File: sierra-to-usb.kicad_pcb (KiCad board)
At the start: 4 copper layers, 140 x 100 mm, 367 parts, among them CN1 EM92xx / RM520N M.2 Key-B (67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, J1 TYPE-C-31-M-04, J10 BWSMA-KE-Z001, J11 CONMHF4-SMD-G-T, J12 BWSMA-KE-Z001, J13 CONMHF4-SMD-G-T, J14 BWSMA-KE-Z001, J15 CONMHF4-SMD-G-T, J16 BWSMA-KE-Z001, J17 CONMHF4-SMD-G-T, J18 BWSMA-KE-Z001, J2 TYPE-C-31-M-12, J3 TYPE-C-31-M-12, J4 SWD, J5 Qwiic, J6 Fan, J7 Spare, J8 2250504-1, J9 CONMHF4-SMD-G-T, Q1 2N7002, Q2 2N7002, Q20 FDMS86250, Q21 FDMC2523P, Q22 BSC057N08NS3 G, Q23 BSC057N08NS3 G, Q24 FCX493TA, Q25 FCX493TA, Q3 2N7002, Q30 IRLR7843TRPBF, Q31 IRLR7843TRPBF, Q32 DMG3415U-7, Q33 DMG3415U-7, Q34 2N7002, Q35 2N7002, Q36 BSS138, Q37 BSS138, Q38 BSS138, Q39 2N7002, Q4 2N7002, Q40 BSS138, Q5 2N7002, SW1 DIP-4, SW2 LED_KILL, SW3 BOOTSEL, SW4 RUN, T1 750313355, U1 HD3SS3220RNHR, U10 TPS23730RMTR, U11 93C46, U12 TLV62569DBVR, U13 INA226AIDGSR, U14 INA226AIDGSR, U15 TPS62933FDRLR, U17 AP2112K-3.3TRG1, U19 LM5050MKX-1/NOPB, U2 CH224K, U20 TCMT1107, U21 LM5050MKX-1/NOPB, U22 TL431IDBVR, U23 FOD817DS, U24 RP2040, U25 W25Q128JVS, U26 TMP112AIDRLR, U27 TMP112AIDRLR, U28 SK6805-EC15, U29 TS3A27518EPWR, U3 TPS565201DDCR, U30 ST4SIM-200M, U4 AP2112K-3.3TRG1, U5 AP2112K-1.8TRG1, U8 TS3USB221DRCR, U9 RTL8125BG-CG, Y1 12MHz, Y2 25MHz

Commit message: pcb/rules: match JLCPCB capabilities + calculator-verified impedance geometry
Netclass recovery: commit 777bcae (KiCad session-quit prefs save) had
clobbered the Task-15 netclasses -- DIFF_USB_90/PCIE_85/MDI_100, RF_50,
POE_PRI, POWER were gone, so every .kicad_dru impedance rule AND the
2.5mm PoE moat matched nothing. Restored all 7 classes + 37 patterns
from 59abbed and dropped the orphaned Sig/USB placeholders (their 50SE/
90D tuning profiles kept, re-attached to Default/DIFF_USB_90).

Impedance geometry re-derived on JLCPCB's live calculator (stackup tab
JLC04161H-7628 Standard, 4L/1.6mm, outer 1oz/inner 0.5oz, 2026-07-16),
closing the PRIORITY RF_50 order gate:
  90D  0.24  -> 0.2474 / 0.15   85D 0.27 -> 0.2835 / 0.15
  100D 0.19  -> 0.1826 / 0.15   RF_50 CPWG 0.14 -> 0.3345 / 0.30 gap
  (closed-form CPWG was 2.4x too narrow; would have run ~70+ ohm)
NEW: Default class = 50 ohm SE microstrip 0.3586mm (user request), with
a DRU opt-width rule allowing neck-downs to the 0.09 fab floor.

Board constraint floors set to the live JLCPCB multilayer capability
table (trace/space 0.09, via 0.25/0.15, hole-to-hole 0.2, edge 0.3,
silk 0.15/1.0mm, mask bridge 0.1 via solder_mask_min_width). DRU
Section 3 adds PTH-specific limits (annular 0.15, hole-to-track 0.28,
pad hole-to-hole 0.45) + scoped exemptions for the USB-C C129018
B-row (JLC's own pattern) and same-footprint pad pairs (0.15 floor).

DFM fixes: J1/CN1 locating pegs converted PTH->NPTH (plating would
have shrunk the holes below the pegs); J8 magjack pads shrunk
(13-16: 1.5->1.35, 1: 1.7->1.55, shields 2.4->2.3) to clear 0.04mm
different-net etch gaps. Lib + board both updated.

Gates: nets/footprints/3d pass, ERC 0 errors, DRC 0 in-board errors
(silk warnings + off-board parking-lot items remain, mid-layout).
docs: ordering.md impedance table rewritten, sourcing.md SIM-CD gate
struck (14c), footprint-verification.md deviation notes.

Co-Authored-By: Claude Fable 5 <noreply@anthropic.com>
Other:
- board text added: "IMPEDANCE GEOMETRIES (L1 top, referenced to In1 GND through 0.2104mm/Er4.4 prepreg). SOURCE: JLCPCB live impedance calculator, stackup JLC04161H-7628 (Standard, finished 1.59mm+/-10%), 4L/1.6mm, outer 1oz / inner 0.5oz, verified 2026-07-16 (replaces Task-15 closed-form values; RF_50 closed form was wrong 2.4x -- see .kicad_dru header): DIFF_USB_90 (USB2 SS/D+-): W=0.2474mm gap=0.15mm -> Zdiff 90 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"
- board text removed: "IMPEDANCE GEOMETRIES (L1 top, referenced to In1 GND, H=0.2104mm Er=4.4; computed via IPC-2141 edge-coupled microstrip / grounded-CPW closed form, T=0.05mm finished outer Cu; verify against JLCPCB's live impedance calculator before ordering): DIFF_USB_90 (USB2 SS/D+-): W=0.24mm gap=0.15mm -> Zdiff ~90.2 ohm DIFF_PCIE_85 (M.2 PCIe/REFCLK): W=0.27mm gap=0.15mm -> Zdiff ~85.0 ohm DIFF_MDI_100 (Ethern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"
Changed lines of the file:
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@@
 		)
 		(pad_to_mask_clearance 0)
+		(solder_mask_min_width 0.1)
 		(allow_soldermask_bridges_in_footprints no)
 		(tenting
@@
 			)
 		)
-		(pad "" thru_hole circle
+		(pad "" np_thru_hole circle
 			(at -3.67 -2.54 180)
 			(size 0.8 0.8)
@@
 			(remove_unused_layers no)
 		)
-		(pad "" thru_hole circle
+		(pad "" np_thru_hole circle
 			(at 3.68 -2.54 180)
 			(size 0.8 0.8)
@@
 			)
 		)
-		(pad "" thru_hole circle
+		(pad "" np_thru_hole circle
 			(at -10 1.5)
 			(size 1.1 1.1)
@@
 			(remove_unused_layers no)
 		)
-		(pad "" thru_hole circle
+		(pad "" np_thru_hole circle
 			(at 10 1.5)
 			(size 1.6 1.6)
@@
 		(pad "1" thru_hole roundrect
 			(at 5.08 -7.945 180)
-			(size 1.7 1.7)
+			(size 1.55 1.55)
 			(drill 0.9)
 			(layers "*.Cu" "*.Mask")
@@
 		(pad "13" thru_hole circle
 			(at 5.588 -0.84 180)
-			(size 1.5 1.5)
+			(size 1.35 1.35)
 			(drill 0.9)
 			(layers "*.Cu" "*.Mask")
@@
 		(pad "14" thru_hole circle
 			(at -5.588 -0.84 180)
-			(size 1.5 1.5)
+			(size 1.35 1.35)
 			(drill 0.9)
 			(layers "*.Cu" "*.Mask")
@@
 		(pad "15" thru_hole circle
 			(at 5.588 0.703 180)
-			(size 1.5 1.5)
+			(size 1.35 1.35)
 			(drill 0.9)
 			(layers "*.Cu" "*.Mask")
@@
 		(pad "16" thru_hole circle
 			(at -5.588 0.703 180)
-			(size 1.5 1.5)
+			(size 1.35 1.35)
 			(drill 0.9)
 			(layers "*.Cu" "*.Mask")
@@
 		(pad "SH" thru_hole oval
 			(at -7.166 -6.189 180)
-			(size 2.4 4.6)
+			(size 2.3 4.6)
 			(drill oval 2 4.2)
 			(layers "*.Cu" "*.Mask")
@@
 		(pad "SH" thru_hole oval
 			(at 7.166 -6.189 180)
-			(size 2.4 4.6)
+			(size 2.3 4.6)
 			(drill oval 2 4.2)
 			(layers "*.Cu" "*.Mask")
@@
 		)
 	)
-	(gr_text "IMPEDANCE GEOMETRIES (L1 top, referenced to In1 GND, H=0.2104mm Er=4.4; computed via\nIPC-2141 edge-coupled microstrip / grounded-CPW closed form, T=0.05mm finished outer Cu;\nverify against JLCPCB's live impedance calculator before ordering):\n  DIFF_USB_90  (USB2 SS/D+-):  W=0.24mm  gap=0.15mm  -> Zdiff ~90.2 ohm\n  DIFF_PCIE_85 (M.2 PCIe/REFCLK): W=0.27mm gap=0.15mm -> Zdiff ~85.0 ohm\n  DIFF_MDI_100 (Ethernet MDI): W=0.19mm  gap=0.15mm  -> Zdiff ~100.1 ohm\n  RF_50 (CPWG, ANT/GNSS):      W=0.14mm  ground-gap=0.30mm -> Z0 ~50.0 ohm\nCopper-to-other-net clearance floor for all 4 classes: 0.30mm (see .kicad_dru).\nAlso entered in docs/ordering.md for the JLC order form."
+	(gr_text "IMPEDANCE GEOMETRIES (L1 top, referenced to In1 GND through 0.2104mm/Er4.4 prepreg).\nSOURCE: JLCPCB live impedance calculator, stackup JLC04161H-7628 (Standard, finished 1.59mm+/-10%),\n4L/1.6mm, outer 1oz / inner 0.5oz, verified 2026-07-16 (replaces Task-15 closed-form values;\nRF_50 closed form was wrong 2.4x -- see .kicad_dru header):\n  DIFF_USB_90  (USB2 SS/D+-):  W=0.2474mm  gap=0.15mm  -> Zdiff 90 ohm\n  DIFF_PCIE_85 (M.2 PCIe/REFCLK): W=0.2835mm gap=0.15mm -> Zdiff 85 ohm\n  DIFF_MDI_100 (Ethernet MDI): W=0.1826mm  gap=0.15mm  -> Zdiff 100 ohm\n  RF_50 (CPWG, ANT/GNSS):      W=0.3345mm  ground-gap=0.30mm -> Z0 50 ohm\n  Default (normal signals):    W=0.3586mm microstrip -> Z0 50 ohm (user-requested)\nCopper-to-other-net clearance floor for the 4 controlled classes: 0.30mm (see .kicad_dru).\nAlso entered in docs/ordering.md for the JLC order form (select JLC04161H-7628 + impedance control)."
 		(at -22.87868 70.12132 0)
 		(layer "Cmts.User")

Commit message: pcb: user F8 netlist update (J2/J3->M-04, SIM->XKNANO) + 85D/100D/50CPWG tuning profiles + XKNANO NPTH pegs
- Board: user GUI session applied Update PCB from Schematic (3x TYPE-C-31-M-04,
  2x NanoSIM_XKB_XKNANO-113; stale M-12/CSIM footprints gone). Session quit-save
  also alphabetized netclasses in the .kicad_pro -- values verified intact.
- Tuning profiles completed: 85D (0.2835/0.15), 100D (0.1826/0.15), 50CPWG
  (0.3345) cloned from the session's 50SE/90D templates with JLCPCB-calculator
  geometry; attached to DIFF_PCIE_85 / DIFF_MDI_100 / RF_50. All 7 classes now
  carry matching profiles (POE_PRI/POWER intentionally none).
- XKNANO-113 0.9mm locating pegs converted thru_hole->np_thru_hole (lib+board),
  same easyeda2kicad plated-peg artifact as J1/CN1.
- KNOWN OPEN (user re-placement): SIM1/SIM2 courtyards overlap at old spacing --
  XKNANO body is larger; SIM2 shell pad currently shorts SIM1 UIM1_CLK pad.

Gates: nets/footprints pass; J8/J1/CN1 geometry fixes verified surviving F8.

Co-Authored-By: Claude Fable 5 <noreply@anthropic.com>
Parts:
- J2, J3: value TYPE-C-31-M-12 -> TYPE-C-31-M-04; footprint Connector_USB:USB_C_Receptacle_HRO_TYPE-C-31-M-12 -> sierra-to-usb:USB_C_Receptacle_HRO_TYPE-C-31-M-04
- SIM1, SIM2: value CSIM-H137-7P -> XKNANO-113; footprint sierra-to-usb:NanoSIM_JXTCONN_CSIM-H137-7P -> sierra-to-usb:NanoSIM_XKB_XKNANO-113
- moved T1 80.1 mm to (192.0, 16.5)
- moved J1 74.6 mm to (-33.4, -8.89)
- moved C58 71.7 mm to (-41.6, 0.08)
- moved C59 71.7 mm to (-41.6, 2.59)
- moved C62 71.7 mm to (-41.6, 10.1)
- moved R71 71.7 mm to (-41.6, 17.6)
- moved C60 71.7 mm to (-41.6, 5.10)
- moved C61 71.7 mm to (-41.6, 7.61)
- moved D20 71.7 mm to (-38.1, 1.07)
- moved D21 71.7 mm to (-35.2, 1.07)
- moved D22 71.7 mm to (-32.3, 1.07)
- moved D23 71.7 mm to (-29.4, 1.07)
- moved D24 71.7 mm to (-35.4, 16.4)
- moved R69 71.7 mm to (-41.6, 12.6)
- moved R70 71.7 mm to (-41.6, 15.1)
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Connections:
- SIM1 pad 4: GND -> UIM1_DET
- SIM1 pad 5: UIM1_IO -> GND
- SIM1 pad 6: GND -> unconnected-(SIM1-VPP-Pad6)
- SIM1 pad 7: UIM1_DET -> UIM1_IO
- SIM2 pad 4: GND -> /SIM/UIM2S_DET
- SIM2 pad 5: /SIM/UIM2S_IO -> GND
- SIM2 pad 6: GND -> unconnected-(SIM2-VPP-Pad6)
- SIM2 pad 7: /SIM/UIM2S_DET -> /SIM/UIM2S_IO

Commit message: pcb: layout progress snapshot (user session, pre-resize)
Co-Authored-By: Claude Fable 5 <noreply@anthropic.com>
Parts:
- C116, C117, C118, C119, C120, C121, C122, C123, C124, C125, U10: moved to B.Cu
- moved J5 243.9 mm to (20.4, 89.5), turned to -90 degrees
- moved U26 243.0 mm to (24.6, 52.2)
- moved U27 243.0 mm to (24.6, 55.4)
- moved SW3 243.0 mm to (20.0, 52.6)
- moved SW4 243.0 mm to (20.0, 57.0)
- moved J3 242.3 mm to (23.1, 79.8), turned to -90 degrees
- moved J7 238.5 mm to (19.2, 64.9)
- moved U25 232.6 mm to (28.0, 61.0)
- moved J4 222.6 mm to (30.0, 79.0)
- moved U8 220.8 mm to (48.0, 67.0)
- moved Q39 220.8 mm to (49.0, 72.0)
- moved D27 202.6 mm to (79.7, 39.9), turned to -90 degrees
- moved J6 200.5 mm to (59.0, 61.0)
- moved U30 195.8 mm to (89.0, 51.0)
- moved C119 192.8 mm to (76.2, 38.8), turned to -90 degrees
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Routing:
- net UIM1_CLK: track 0.00 -> 8.91 mm, vias 0 -> 1
- net /SIM/UIM2S_IO: track 0.00 -> 8.63 mm, vias 0 -> 1
- net UIM1_IO: track 0.00 -> 8.46 mm, vias 0 -> 1
- net /SIM/UIM2S_CLK: track 0.00 -> 7.76 mm, vias 0 -> 1
- net /SIM/UIM2S_DET: track 0.00 -> 7.48 mm, vias 0 -> 1
- net UIM1_DET: track 0.00 -> 7.33 mm, vias 0 -> 1
- net /SIM/UIM2S_VDD: track 0.00 -> 5.37 mm, vias 0 -> 2
- net UIM1_VDD: track 0.00 -> 5.17 mm, vias 0 -> 2
- net /SIM/UIM2S_RST: track 0.00 -> 4.30 mm, vias 0 -> 1
- net UIM1_RST: track 0.00 -> 4.09 mm, vias 0 -> 1

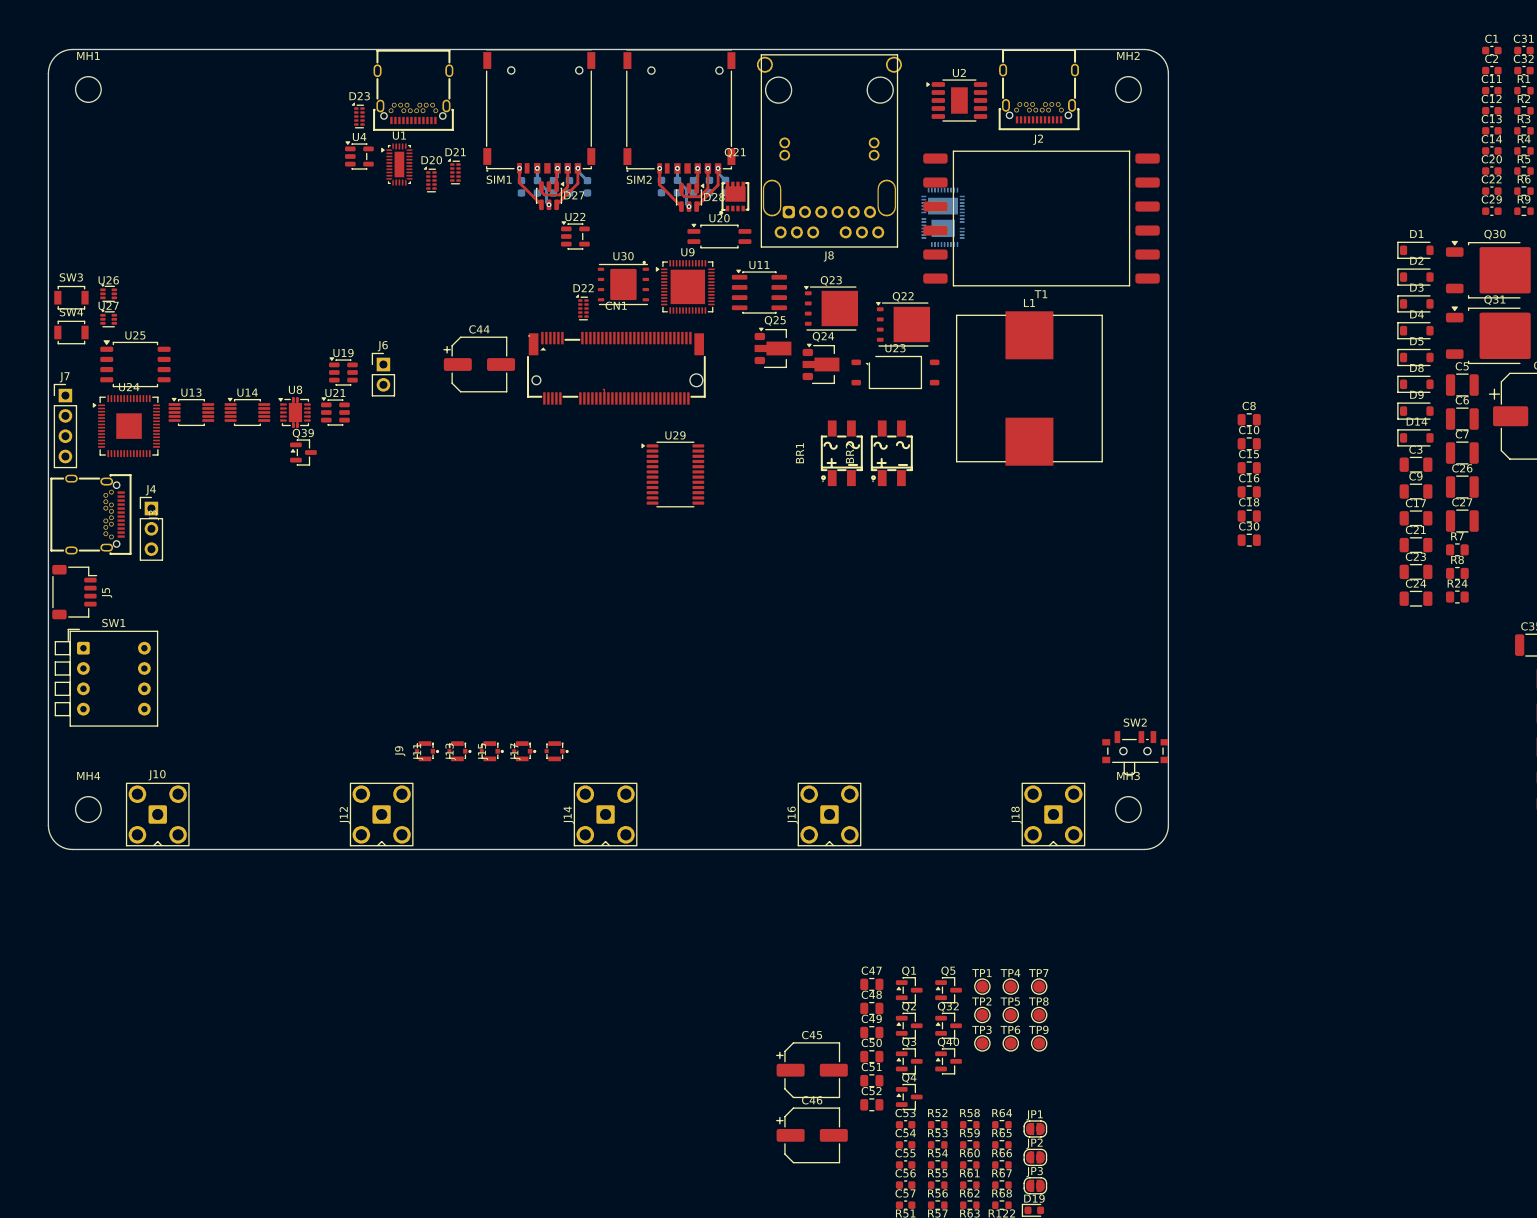
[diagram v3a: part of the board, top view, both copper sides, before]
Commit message: pcb: resize board 140x100 -> 180x140 (dev-board decision), corner MHs relocated
Outline right edge +40mm (x=197.12), bottom edge +40mm (y=161.62), top-left
anchored; corner radius arcs preserved. MH2/MH3/MH4 keep 5mm insets from
their new corners. Board is now a standoff-mounted dev board (no enclosure);
next iteration repackages. Former edge parts (SMA row J10-J18, SW2, J3) now
float mid-board pending user re-placement.

Co-Authored-By: Claude Fable 5 <noreply@anthropic.com>
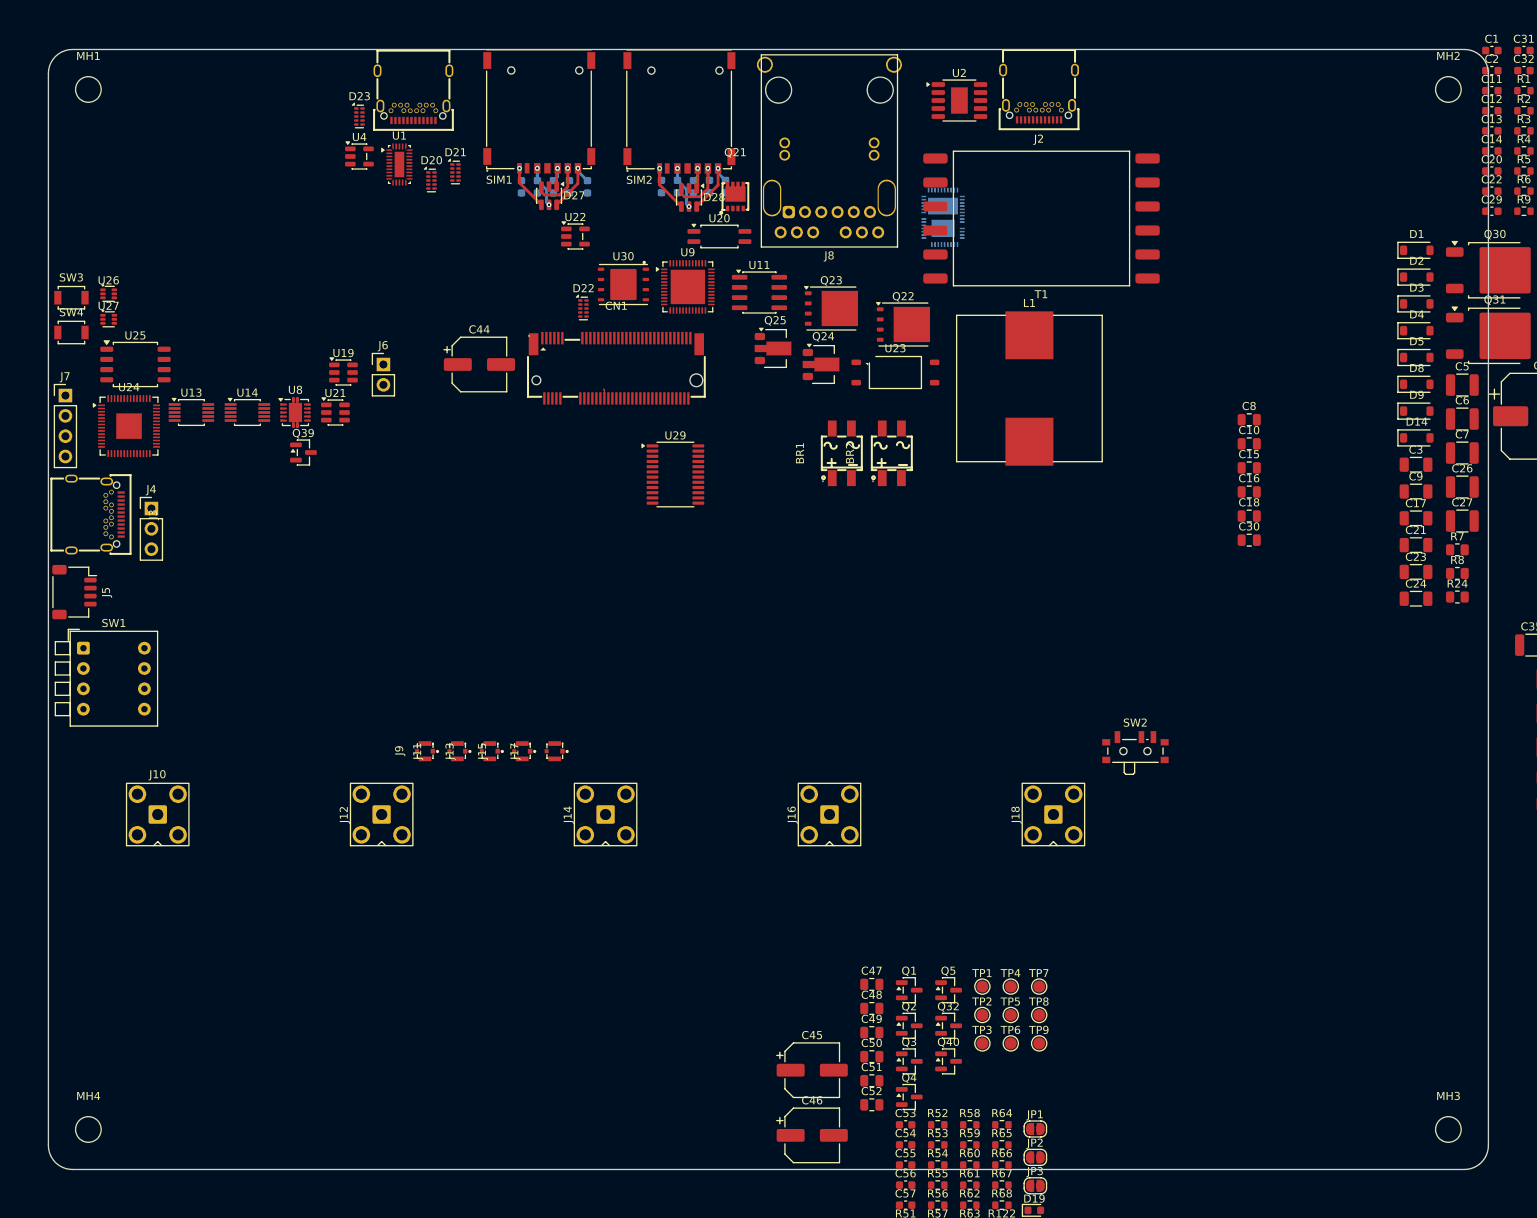
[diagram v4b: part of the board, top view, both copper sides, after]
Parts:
- moved MH3 56.6 mm to (192.1, 156.6)
- moved MH2 40.0 mm to (192.1, 26.6)
- moved MH4 40.0 mm to (22.1, 156.6)
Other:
- board size 140 x 100 mm -> 180 x 140 mm
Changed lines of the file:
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@@
 		(locked yes)
 		(layer "F.Cu")
-		(at 22.12132 116.62132)
+		(at 22.12132 156.62132)
 		(descr "Mounting Hole 3.2mm, M3, no annular, generated by kicad-footprint-generator mountinghole.py")
 		(tags "mountinghole M3")
@@
 		(locked yes)
 		(layer "F.Cu")
-		(at 152.12132 26.62132)
+		(at 192.12132 26.62132)
 		(descr "Mounting Hole 3.2mm, M3, no annular, generated by kicad-footprint-generator mountinghole.py")
 		(tags "mountinghole M3")
@@
 		(locked yes)
 		(layer "F.Cu")
-		(at 152.12132 116.62132)
+		(at 192.12132 156.62132)
 		(descr "Mounting Hole 3.2mm, M3, no annular, generated by kicad-footprint-generator mountinghole.py")
 		(tags "mountinghole M3")
@@
 	)
 	(gr_line
-		(start 17.12132 118.62132)
+		(start 17.12132 158.62132)
 		(end 17.12132 24.62132)
 		(stroke
@@
 	(gr_line
 		(start 20.12132 21.62132)
-		(end 154.12132 21.62132)
+		(end 194.12132 21.62132)
 		(stroke
 			(width 0.1)
@@
 	)
 	(gr_arc
-		(start 20.12132 121.62132)
-		(mid 18 120.74264)
-		(end 17.12132 118.62132)
+		(start 20.12132 161.62132)
+		(mid 18 160.74264)
+		(end 17.12132 158.62132)
 		(stroke
 			(width 0.1)
@@
 	)
 	(gr_arc
-		(start 154.12132 21.62132)
-		(mid 156.24264 22.5)
-		(end 157.12132 24.62132)
+		(start 194.12132 21.62132)
+		(mid 196.24264 22.5)
+		(end 197.12132 24.62132)
 		(stroke
 			(width 0.1)
@@
 	)
 	(gr_line
-		(start 154.12132 121.62132)
-		(end 20.12132 121.62132)
+		(start 194.12132 161.62132)
+		(end 20.12132 161.62132)
 		(stroke
 			(width 0.1)
@@
 	)
 	(gr_line
-		(start 157.12132 24.62132)
-		(end 157.12132 118.62132)
+		(start 197.12132 24.62132)
+		(end 197.12132 158.62132)
 		(stroke
 			(width 0.1)
@@
 	)
 	(gr_arc
-		(start 157.12132 118.62132)
-		(mid 156.24264 120.74264)
-		(end 154.12132 121.62132)
+		(start 197.12132 158.62132)
+		(mid 196.24264 160.74264)
+		(end 194.12132 161.62132)
 		(stroke
 			(width 0.1)
